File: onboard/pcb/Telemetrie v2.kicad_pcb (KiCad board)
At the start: 4 copper layers, 100 x 91 mm, 78 parts, among them J1 Conn_02x03_Odd_Even, J2 Conn_01x02_Pin, J3 SMA SMD, J4 Conn_01x04_Pin, J5 Conn_01x02_Pin, M1 Conn_01x01_Pin, M2 Conn_01x01_Pin, M3 Conn_01x01_Pin, M4 Conn_01x01_Pin, U1 AVR128DB64x-xPT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

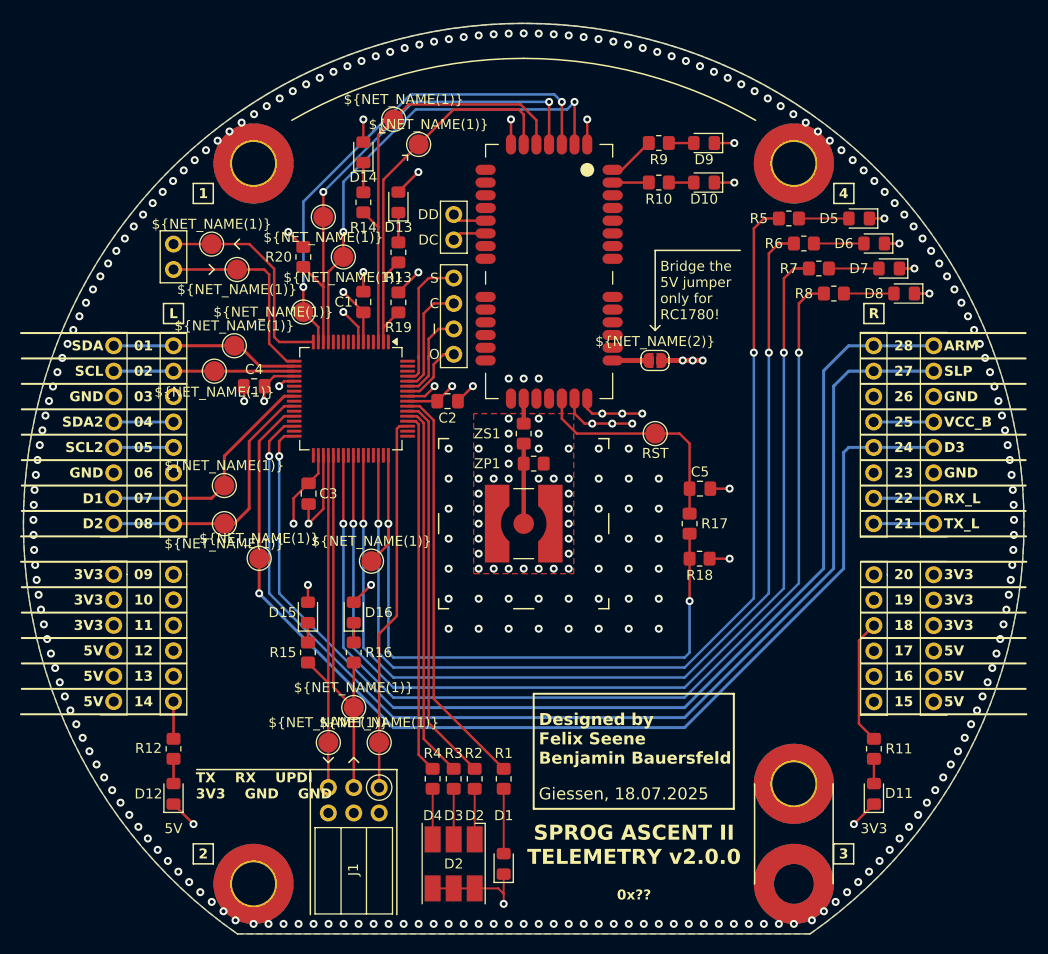
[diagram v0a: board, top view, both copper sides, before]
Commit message: adjusted schematic and pcb according to the design rule check
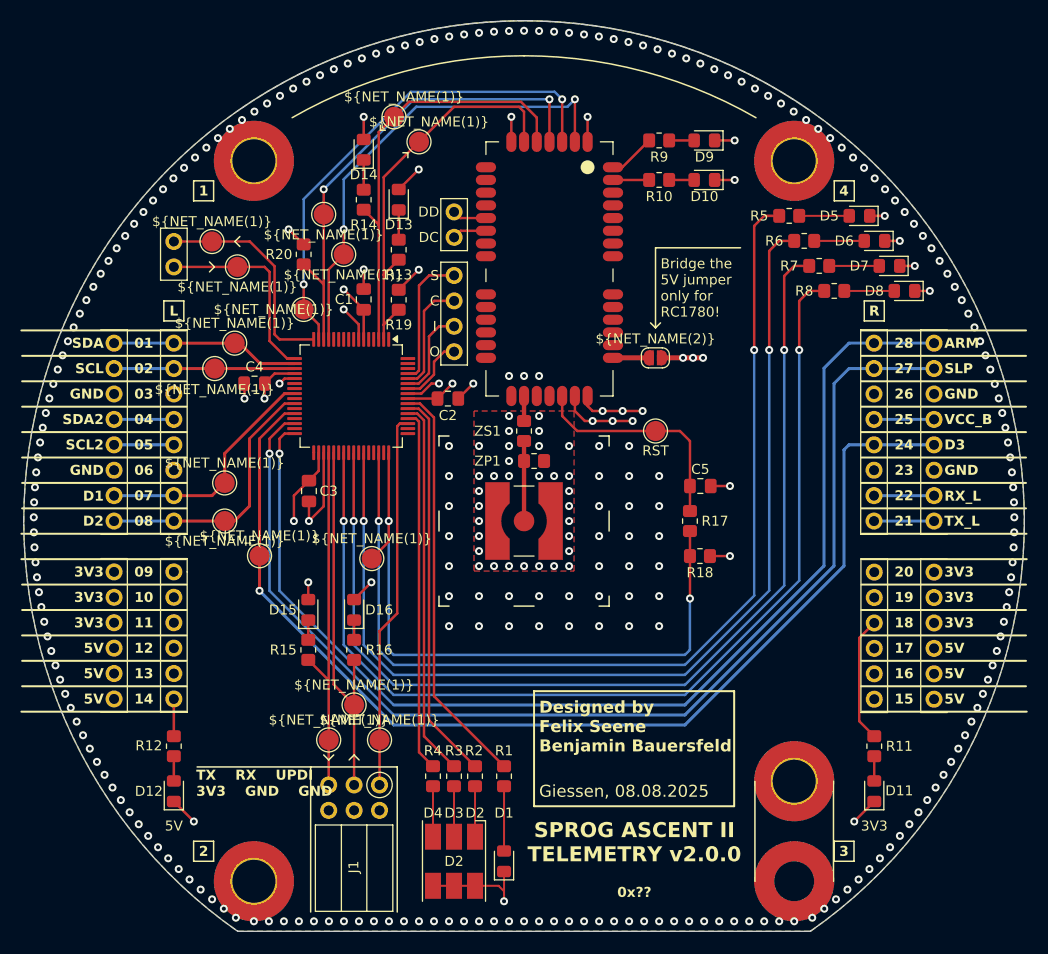
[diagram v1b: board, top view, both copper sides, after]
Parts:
- moved M3 0.26 mm to (27.0, 25.7)
- moved R5 0.26 mm to (26.5, -30.8)
- moved R6 0.26 mm to (28.0, -28.3)
- moved R7 0.26 mm to (29.5, -25.8)
- moved R8 0.26 mm to (31.0, -23.3)
- moved TP7 0.26 mm to (-14.4, 21.6)
- moved TP9 0.26 mm to (-17.0, 18.1)
- moved R2 0.26 mm to (-4.87, 25.2)
- moved R3 0.26 mm to (-6.97, 25.2)
- moved R1 0.26 mm to (-1.97, 25.2)
- moved C1 0.26 mm to (-16.0, -22.4)
- moved R4 0.26 mm to (-9.07, 25.2)
- moved D11 0.26 mm to (35.0, 26.7)
- moved D12 0.26 mm to (-35.0, 26.7)
- moved D5 0.26 mm to (33.6, -30.8)
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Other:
- board text added: "Giessen, 08.08.2025"
- board text removed: "Giessen, 18.07.2025"

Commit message: prep for production version
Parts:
- added LS1: CMT-0525-75-SMT-TR, Footprints:XDCR_CMT-0525-75-SMT-TR, F.Cu at (-27.9, 18.2)
- added R21: 5k6, Resistor_SMD:R_0805_2012Metric_Pad1.20x1.40mm_HandSolder, F.Cu at (30.0, -18.8)
- moved D11 0.26 mm to (35.0, 27.0)
- moved D12 0.26 mm to (-35.0, 27.0)
- moved D16 0.26 mm to (-17.0, 8.87)
- moved J5 0.26 mm to (-35.0, -27.9)
- moved JL1 0.26 mm to (-35.0, -17.8)
- moved JR1 0.26 mm to (35.0, -17.8)
- moved JR2 0.26 mm to (35.0, 5.10)
- moved JR3 0.26 mm to (41.0, -17.8)
- moved JR4 0.26 mm to (41.0, 5.10)
- moved R11 0.26 mm to (35.0, 22.5)
- moved R12 0.26 mm to (-35.0, 22.5)
- moved R16 0.26 mm to (-17.0, 12.9)
- moved TP9 0.26 mm to (-17.0, 18.4)
- moved C1 0.26 mm to (-16.0, -22.2)
- moved D13 0.26 mm to (-12.5, -32.1)
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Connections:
- U1 pad 12: unconnected-(U1-PB4-Pad12) -> Net-(U1-PB4)
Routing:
- net Net-(U1-PB4): track 0.00 -> 38.5 mm
- net GND: track 61.5 -> 65.9 mm, vias 294 -> 296
- net ARM: track 113.6 -> 116.1 mm, vias 1 -> 2
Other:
- board text added: "0x10"
- board text added: "Giessen, 20.08.2025"
- board text added: "JLCJLCJLCJLC"
- board text added: "Licensed under CERN-OHL-S v2 or any later version: ohwr.org/cern_ohl_s_v2.txt The sources files can be found at: github.com/Spaceflight-Rocketry-Giessen-e-V/Telemetry"
- board text added: "SPROG ASCENT II TELEMETRY v0.0.1"
- board text removed: "0x??"
- board text removed: "Designed by Felix Seene Benjamin Bauersfeld"
- board text removed: "Giessen, 08.08.2025"
- board text removed: "SPROG ASCENT II TELEMETRY v2.0.0"

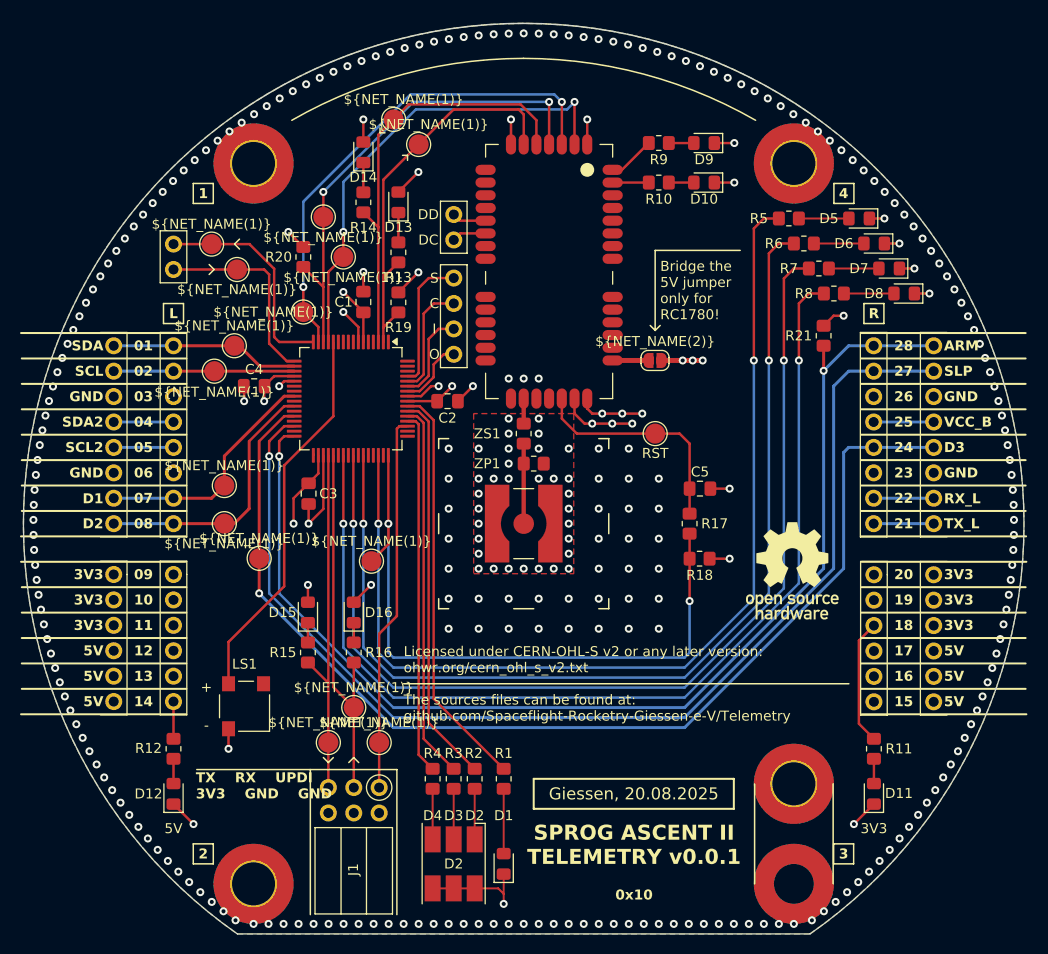
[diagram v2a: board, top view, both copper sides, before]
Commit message: updated custom libraries and silkscreen
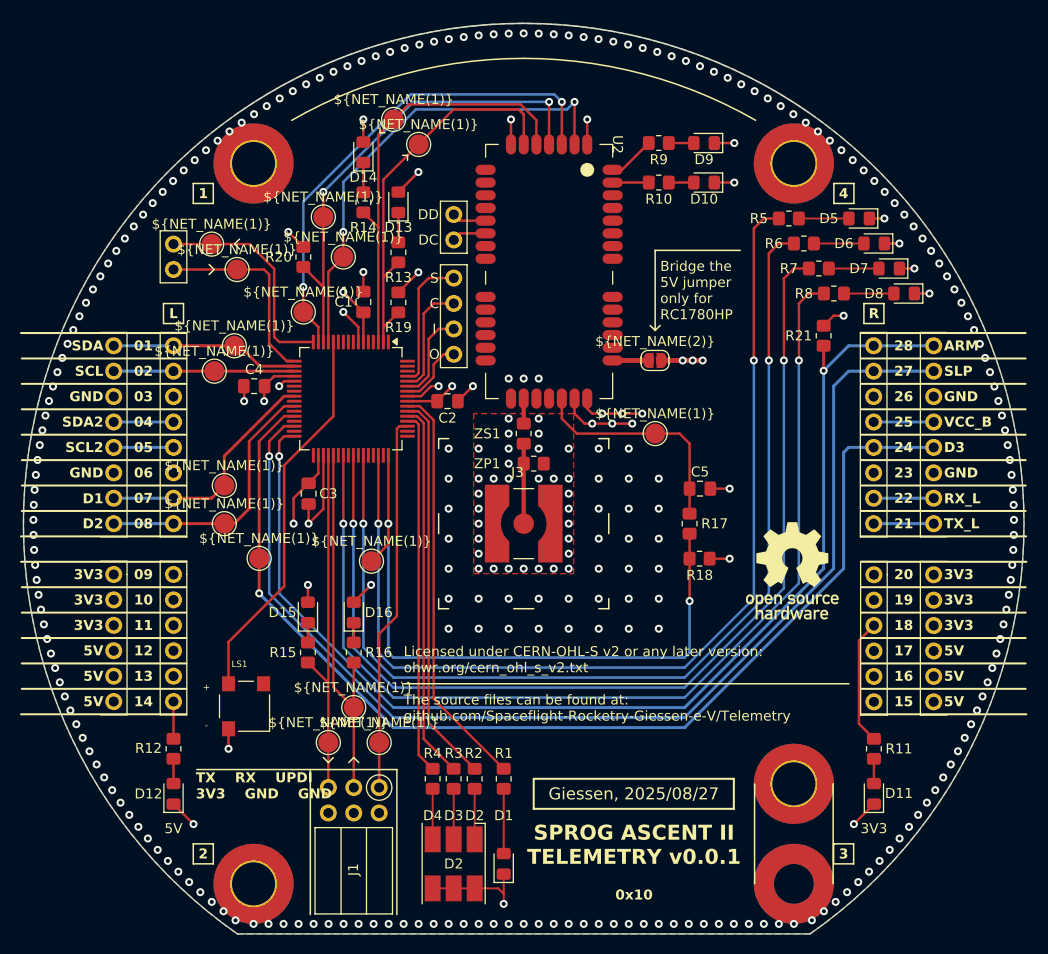
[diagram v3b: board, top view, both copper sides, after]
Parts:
- J3: footprint Footprints:SMA_connector_smd -> Footprints:SMA Connector CONSMA001-SMD-G-T
- JP1: footprint Footprints:Jumper -> Footprints:Solder Jumper
- LS1: footprint Footprints:XDCR_CMT-0525-75-SMT-TR -> Footprints:Buzzer XDCR_CMT-0525-75-SMT-TR
- M1, M2, M3, M4: footprint Footprints:m4hole -> Footprints:M4 Mounting Hole
- TP1, TP10, TP11, TP12, TP13, TP14, TP15, TP16, TP17, TP2, TP3, TP4, TP5, TP6, TP7, TP8, TP9: footprint Footprints:TestPoint -> Footprints:Test Point
- U2: footprint Footprints:RC1780HP -> Footprints:Radiocrafts RC1780HP-RC232
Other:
- board text added: "Bridge the 5V jumper only for RC1780HP"
- board text added: "Giessen, 2025/08/27"
- board text added: "Licensed under CERN-OHL-S v2 or any later version: ohwr.org/cern_ohl_s_v2.txt The source files can be found at: github.com/Spaceflight-Rocketry-Giessen-e-V/Telemetry"
- board text removed: "Bridge the 5V jumper only for RC1780!"
- board text removed: "Giessen, 20.08.2025"
- board text removed: "Licensed under CERN-OHL-S v2 or any later version: ohwr.org/cern_ohl_s_v2.txt The sources files can be found at: github.com/Spaceflight-Rocketry-Giessen-e-V/Telemetry"
